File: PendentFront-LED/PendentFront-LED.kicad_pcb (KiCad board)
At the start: 2 copper layers, 25.7 x 39.2 mm, 98 parts, among them J1 Conn_01x05_Pin, U1 74VHC9595FT, U2 74VHC9595FT, U3 74VHC9595FT, U4 74VHC9595FT

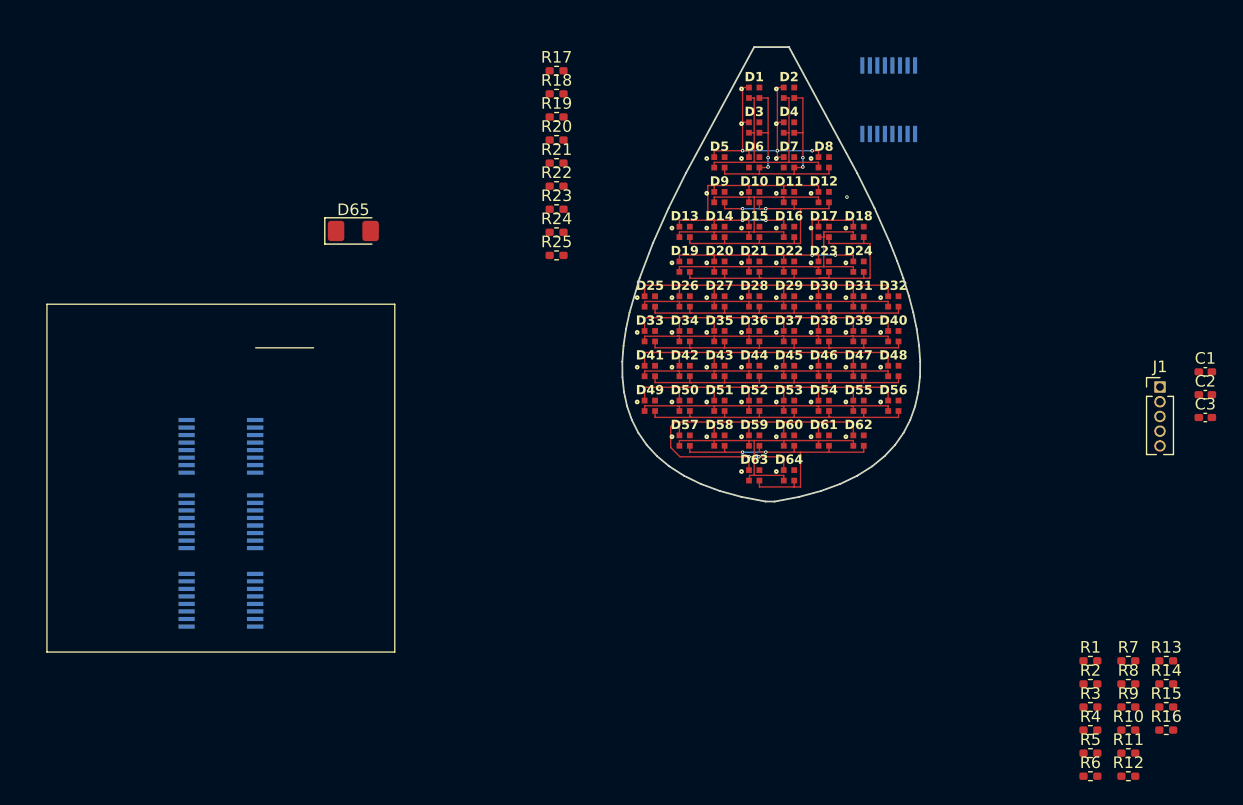
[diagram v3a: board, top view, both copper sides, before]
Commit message: Connected up shift registers. Still need to rearrange connections to make routing possible
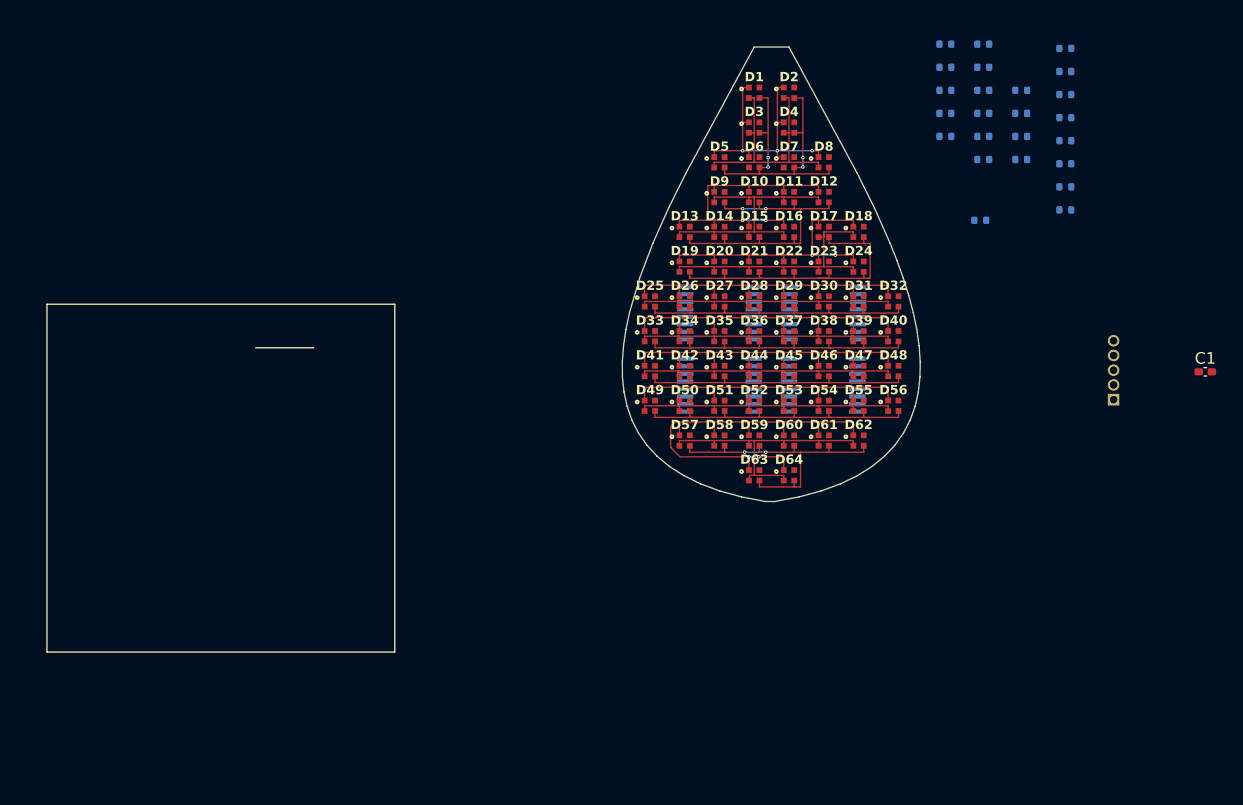
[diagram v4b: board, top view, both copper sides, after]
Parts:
- removed C2, C3: 1uF, Capacitor_SMD:C_0402_1005Metric_Pad0.74x0.62mm_HandSolder
- removed D65: AUX, LED_SMD:LED_1206_3216Metric_Pad1.42x1.75mm_HandSolder
- removed R25: R, Resistor_SMD:R_0402_1005Metric_Pad0.72x0.64mm_HandSolder
- J1: moved to B.Cu
- R1, R10, R11, R12, R13, R14, R15, R16, R17, R18, R19, R2, R20, R21, R22, R23, R24, R3, R4, R5, R6, R7, R8, R9: footprint Resistor_SMD:R_0402_1005Metric_Pad0.72x0.64mm_HandSolder -> Resistor_SMD:R_0402_1005Metric; moved to B.Cu
- moved R12 64.4 mm to (132.8, 47.8)
- moved R6 64.4 mm to (129.5, 47.8)
- moved R11 60.5 mm to (132.8, 49.8)
- moved R5 60.5 mm to (129.5, 49.8)
- moved R10 56.6 mm to (132.8, 51.8)
- moved R16 56.6 mm to (136.0, 51.8)
- moved R4 56.6 mm to (129.5, 51.8)
- moved U3 53.3 mm to (119.0, 77.2), turned to 180 degrees
- moved U4 53.3 mm to (119.0, 71.0), turned to 180 degrees
- moved R9 52.7 mm to (132.8, 53.8)
- moved R15 52.7 mm to (136.0, 53.8)
- moved R3 52.7 mm to (129.5, 53.8)
- moved U2 49.6 mm to (110.0, 71.0), turned to 180 degrees
- moved R14 48.9 mm to (136.0, 55.8)
- moved R2 48.9 mm to (129.5, 55.8)
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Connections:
- U1 pad 10: unconnected-(U1-Q5-Pad10) -> /ROW5
- U1 pad 11: unconnected-(U1-Q6-Pad11) -> /ROW6
- U1 pad 12: unconnected-(U1-Q7-Pad12) -> /ROW7
- U1 pad 13: unconnected-(U1-Q8-Pad13) -> /ROW8
- U1 pad 5: unconnected-(U1-Q1-Pad5) -> /ROW1
- U1 pad 6: unconnected-(U1-Q2-Pad6) -> /ROW2
- U1 pad 7: unconnected-(U1-Q3-Pad7) -> /ROW3
- U1 pad 9: unconnected-(U1-Q4-Pad9) -> /ROW4
- U2 pad 10: unconnected-(U2-Q5-Pad10) -> /COLOR.RED5
- U2 pad 11: unconnected-(U2-Q6-Pad11) -> /COLOR.RED6
- U2 pad 12: unconnected-(U2-Q7-Pad12) -> /COLOR.RED7
- U2 pad 13: unconnected-(U2-Q8-Pad13) -> /COLOR.RED8
- U2 pad 5: unconnected-(U2-Q1-Pad5) -> /COLOR.RED1
- U2 pad 6: unconnected-(U2-Q2-Pad6) -> /COLOR.RED2
- U2 pad 7: unconnected-(U2-Q3-Pad7) -> /COLOR.RED3
- U2 pad 9: unconnected-(U2-Q4-Pad9) -> /COLOR.RED4
- U3 pad 10: unconnected-(U3-Q5-Pad10) -> /COLOR.GREEN5
- U3 pad 11: unconnected-(U3-Q6-Pad11) -> /COLOR.GREEN6
- U3 pad 12: unconnected-(U3-Q7-Pad12) -> /COLOR.GREEN7
- U3 pad 13: unconnected-(U3-Q8-Pad13) -> /COLOR.GREEN8
- U3 pad 5: unconnected-(U3-Q1-Pad5) -> /COLOR.GREEN1
- U3 pad 6: unconnected-(U3-Q2-Pad6) -> /COLOR.GREEN2
- U3 pad 7: unconnected-(U3-Q3-Pad7) -> /COLOR.GREEN3
- U3 pad 9: unconnected-(U3-Q4-Pad9) -> /COLOR.GREEN4
- U4 pad 10: unconnected-(U4-Q5-Pad10) -> /COLOR.BLUE5
- U4 pad 11: unconnected-(U4-Q6-Pad11) -> /COLOR.BLUE6
- U4 pad 12: unconnected-(U4-Q7-Pad12) -> /COLOR.BLUE7
- U4 pad 13: unconnected-(U4-Q8-Pad13) -> /COLOR.BLUE8
- U4 pad 5: unconnected-(U4-Q1-Pad5) -> /COLOR.BLUE1
- U4 pad 6: unconnected-(U4-Q2-Pad6) -> /COLOR.BLUE2
- U4 pad 7: unconnected-(U4-Q3-Pad7) -> /COLOR.BLUE3
- U4 pad 9: unconnected-(U4-Q4-Pad9) -> /COLOR.BLUE4
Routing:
- net (no net): vias 1 -> 0

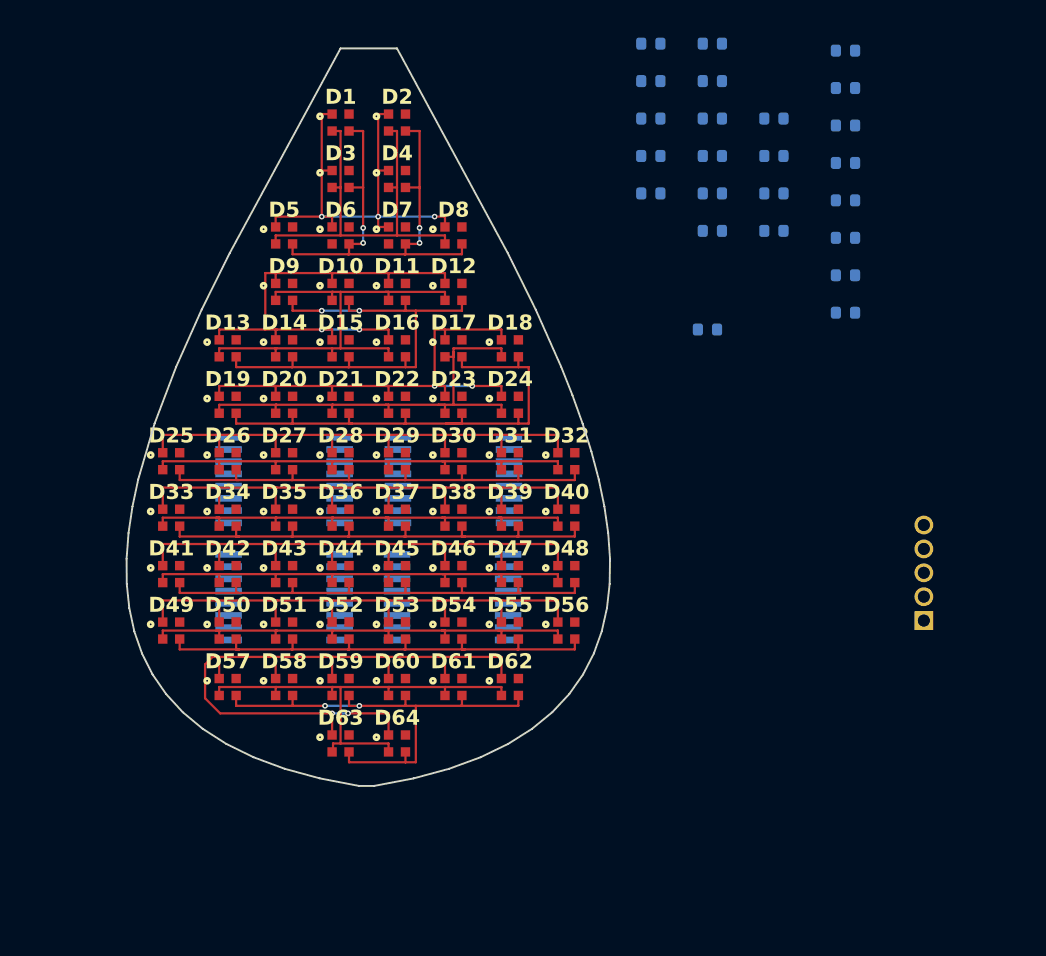
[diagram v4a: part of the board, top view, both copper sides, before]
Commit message: More work on routing the front LED panel
Got through 2 1/2 groups of LEDs and reconfigured connections to shift registers to make routing easier. Split header into 2 groups for easier placement
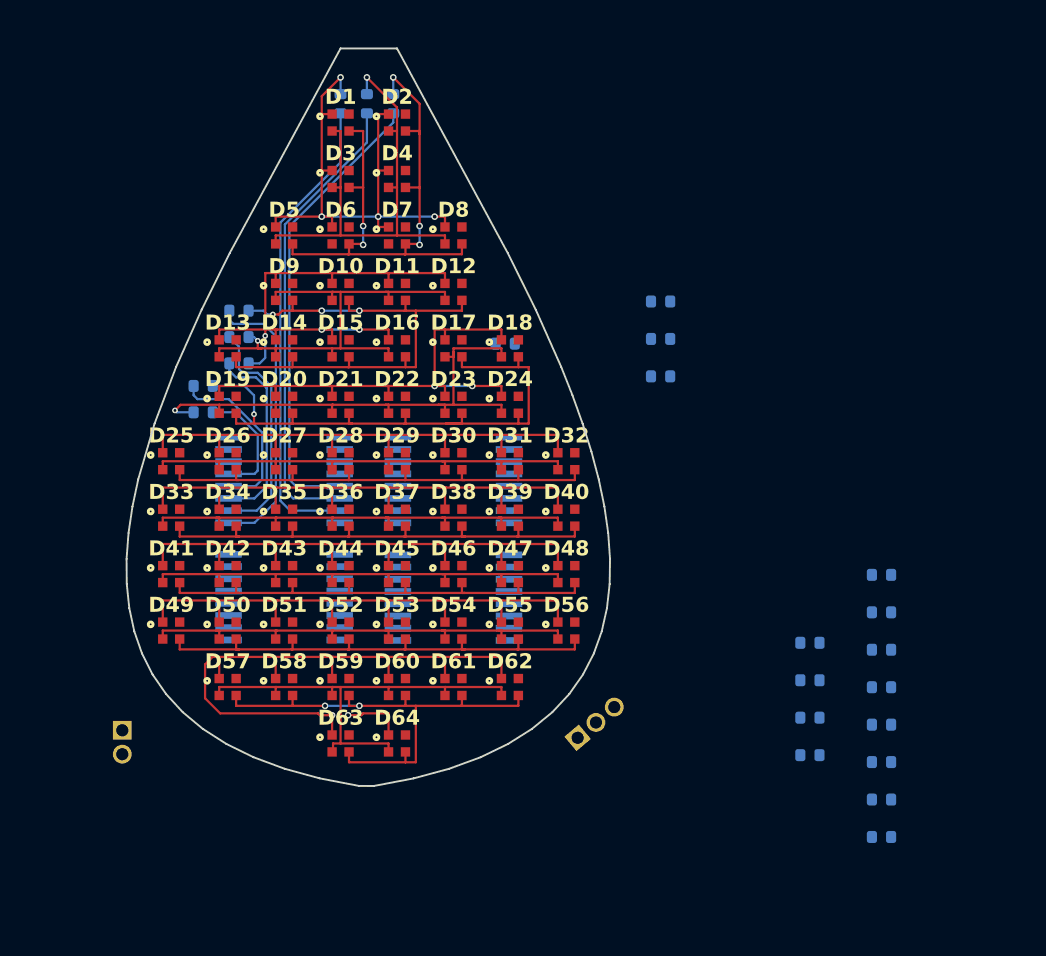
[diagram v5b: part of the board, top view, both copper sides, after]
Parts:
- added J2: Conn_01x02_Pin, Connector_PinHeader_1.27mm:PinHeader_1x02_P1.27mm_Vertical, B.Cu at (101.4, 84.3)
- J1: value Conn_01x05_Pin -> Conn_01x03_Pin; footprint Connector_PinHeader_1.27mm:PinHeader_1x05_P1.27mm_Vertical -> Connector_PinHeader_1.27mm:PinHeader_1x03_P1.27mm_Vertical
- moved R9 29.7 mm to (105.7, 66.0), turned to 180 degrees
- moved R8 29.5 mm to (105.7, 67.4)
- moved R13 27.9 mm to (137.9, 85.6)
- moved R16 27.9 mm to (137.9, 79.7)
- moved R18 27.9 mm to (141.8, 88.0)
- moved R21 27.9 mm to (141.8, 82.0)
- moved R24 27.9 mm to (141.8, 76.0)
- moved R15 27.9 mm to (137.9, 81.6)
- moved R17 27.9 mm to (141.8, 90.0)
- moved R20 27.9 mm to (141.8, 84.0)
- moved R22 27.9 mm to (141.8, 80.0)
- moved R23 27.9 mm to (141.8, 78.0)
- moved R14 27.9 mm to (137.9, 83.6)
- moved R19 27.9 mm to (141.8, 86.0)
- moved R6 26.1 mm to (107.6, 62.0), turned to 180 degrees
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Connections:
- J1 pad 1: VCC -> SerialIn
- J1 pad 2: CLK -> RCK
- J1 pad 3: RCK -> CLK
- U1 pad 3: CLK -> RCK
- U2 pad 10: /COLOR.RED5 -> /COLOR.GREEN2
- U2 pad 11: /COLOR.RED6 -> /COLOR.BLUE2
- U2 pad 12: /COLOR.RED7 -> /COLOR.RED3
- U2 pad 13: /COLOR.RED8 -> /COLOR.GREEN3
- U2 pad 3: CLK -> RCK
- U2 pad 6: /COLOR.RED2 -> /COLOR.GREEN1
- U2 pad 7: /COLOR.RED3 -> /COLOR.BLUE1
- U2 pad 9: /COLOR.RED4 -> /COLOR.RED2
- U3 pad 10: /COLOR.GREEN5 -> /COLOR.RED5
- U3 pad 11: /COLOR.GREEN6 -> /COLOR.GREEN5
- U3 pad 12: /COLOR.GREEN7 -> /COLOR.BLUE5
- U3 pad 13: /COLOR.GREEN8 -> /COLOR.RED6
- U3 pad 3: CLK -> RCK
- U3 pad 5: /COLOR.GREEN1 -> /COLOR.BLUE3
- U3 pad 6: /COLOR.GREEN2 -> /COLOR.RED4
- U3 pad 7: /COLOR.GREEN3 -> /COLOR.GREEN4
- U3 pad 9: /COLOR.GREEN4 -> /COLOR.BLUE4
- U4 pad 10: /COLOR.BLUE5 -> /COLOR.BLUE7
- U4 pad 11: /COLOR.BLUE6 -> /COLOR.RED8
- U4 pad 12: /COLOR.BLUE7 -> /COLOR.GREEN8
- U4 pad 3: CLK -> RCK
- U4 pad 5: /COLOR.BLUE1 -> /COLOR.GREEN6
- U4 pad 6: /COLOR.BLUE2 -> /COLOR.BLUE6
- U4 pad 7: /COLOR.BLUE3 -> /COLOR.RED7
- U4 pad 9: /COLOR.BLUE4 -> /COLOR.GREEN7
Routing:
- net /COLOR.BLUE1: track 0.00 -> 25.3 mm
- net /COLOR.GREEN1: track 0.00 -> 24.9 mm
- net /COLOR.RED1: track 0.00 -> 24.6 mm
- net /COLOR.RED2: track 0.00 -> 15.1 mm
- net /COLOR.GREEN2: track 0.00 -> 12.4 mm
- net /COLOR.BLUE2: track 0.00 -> 10.3 mm
- net /COLOR.RED3: track 0.00 -> 9.38 mm
- net /COLOR.GREEN3: track 0.00 -> 6.42 mm
- net Net-(D1-Pad3): track 27.8 -> 32.4 mm, vias 4 -> 5
- net Net-(D1-Pad2): track 22.8 -> 27.2 mm, vias 0 -> 1
- net Net-(D17-Pad3): track 27.6 -> 31.5 mm, vias 0 -> 1
- net Net-(D17-Pad2): track 25.0 -> 28.5 mm, vias 0 -> 1
- net Net-(D1-Pad1): track 25.5 -> 28.7 mm, vias 3 -> 4
- net Net-(D10-Pad1): track 26.7 -> 29.2 mm, vias 2 -> 3
- net Net-(D10-Pad3): track 26.7 -> 29.2 mm, vias 2 -> 3
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
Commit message: routing
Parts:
- moved R12 9.50 mm to (121.5, 65.8)
- moved R10 8.94 mm to (121.5, 62.8), turned to 180 degrees
- moved R11 8.53 mm to (121.5, 64.2)
- moved R7 3.51 mm to (121.5, 67.2)
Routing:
- net /COLOR.BLUE4: track 0.00 -> 14.3 mm
- net /COLOR.GREEN4: track 0.00 -> 12.4 mm
- net /COLOR.RED4: track 0.00 -> 10.6 mm
- net Net-(D25-Pad3): track 25.9 -> 34.2 mm, vias 0 -> 1
- net /COLOR.BLUE3: track 0.00 -> 7.85 mm
- net Net-(D25-Pad2): track 25.3 -> 32.3 mm, vias 0 -> 1
- net Net-(D25-Pad1): track 29.5 -> 36.3 mm, vias 0 -> 1
- net Net-(D17-Pad1): track 27.0 -> 28.3 mm, vias 2 -> 1
- net Net-(D17-Pad2): track 28.5 -> 28.8 mm, vias 1 -> 3

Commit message: More routing
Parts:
- moved R24 26.3 mm to (119.8, 90.6)
- moved R23 24.4 mm to (119.9, 89.0)
- moved R19 24.3 mm to (118.0, 80.8), turned to 180 degrees
- moved R20 23.8 mm to (118.0, 82.2), turned to 180 degrees
- moved R22 22.4 mm to (120.4, 86.8)
- moved C1 21.2 mm to (130.8, 74.8)
- moved R17 20.8 mm to (125.0, 77.6), turned to 180 degrees
- moved R21 20.6 mm to (121.2, 80.8), turned to 180 degrees
- moved R18 20.5 mm to (125.0, 76.2), turned to 180 degrees
- moved R13 18.8 mm to (125.0, 72.0), turned to 180 degrees
- moved J1 16.5 mm to (109.1, 84.5), turned to 62.5 degrees
- moved R14 16.5 mm to (125.0, 73.4), turned to 180 degrees
- moved R15 14.6 mm to (125.0, 74.8), turned to 180 degrees
- moved R16 13.0 mm to (125.0, 79.0), turned to 180 degrees
- moved J2 4.35 mm to (104.6, 81.4), turned to 35 degrees
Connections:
- U3 pad 13: /COLOR.RED6 -> /COLOR.BLUE4
- U3 pad 9: /COLOR.BLUE4 -> /COLOR.RED6
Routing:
- net VCC: track 0.00 -> 18.0 mm
- net /COLOR.BLUE5: track 0.00 -> 10.6 mm
- net /COLOR.GREEN5: track 0.00 -> 9.66 mm
- net /COLOR.RED6: track 0.00 -> 9.65 mm
- net /COLOR.RED5: track 0.00 -> 9.34 mm
- net Net-(D41-Pad1): track 30.6 -> 37.9 mm, vias 0 -> 1
- net Net-(D57-Pad1): track 36.6 -> 29.8 mm, vias 2 -> 3
- net Net-(D41-Pad2): track 25.3 -> 29.6 mm, vias 0 -> 1
- net /COLOR.GREEN7: track 0.00 -> 3.96 mm
- net Net-(D49-Pad2): track 25.3 -> 28.7 mm, vias 0 -> 1
- net Net-(D49-Pad1): track 30.6 -> 33.8 mm, vias 0 -> 1
- net /COLOR.BLUE7: track 0.00 -> 3.12 mm
- net /COLOR.RED7: track 0.00 -> 2.93 mm
- net /COLOR.BLUE6: track 0.00 -> 2.86 mm
- net Net-(D33-Pad2): track 25.3 -> 27.9 mm, vias 0 -> 1
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
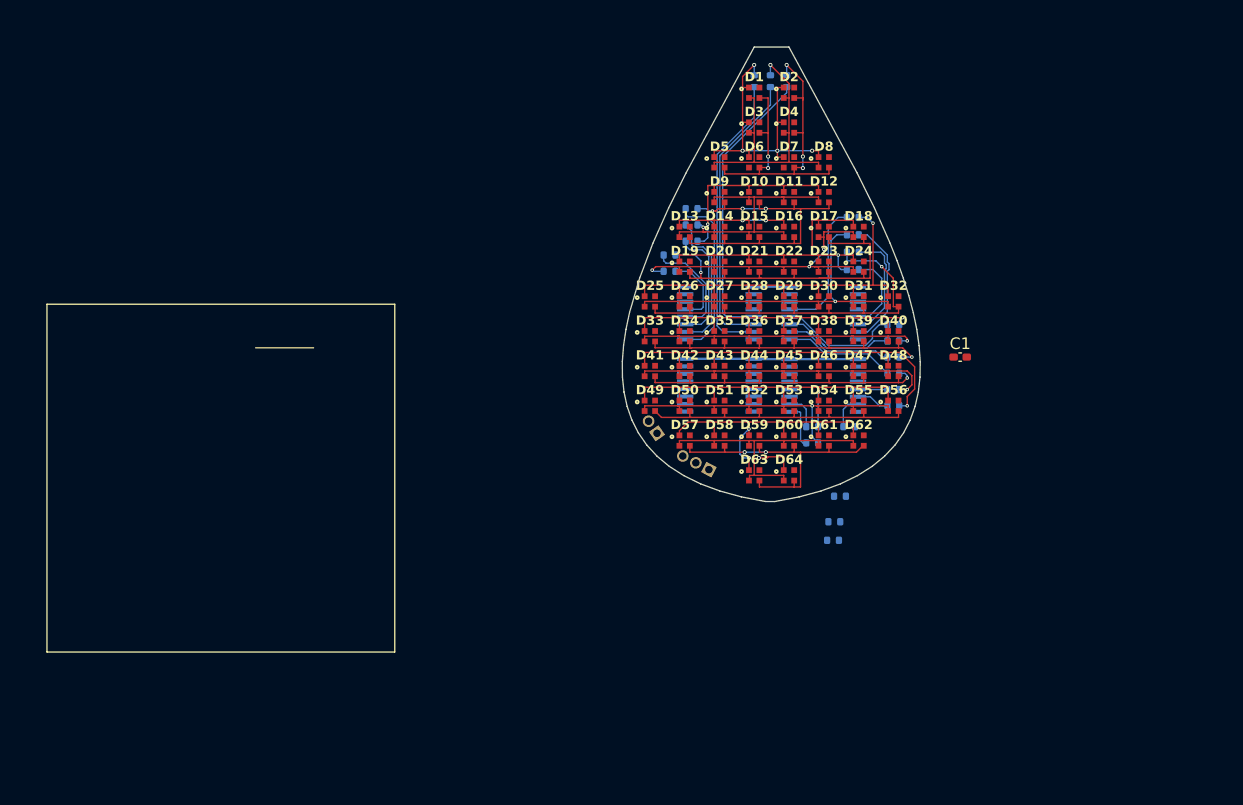
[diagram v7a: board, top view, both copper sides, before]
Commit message: More routing, started putting row lines around the outside of the pendent
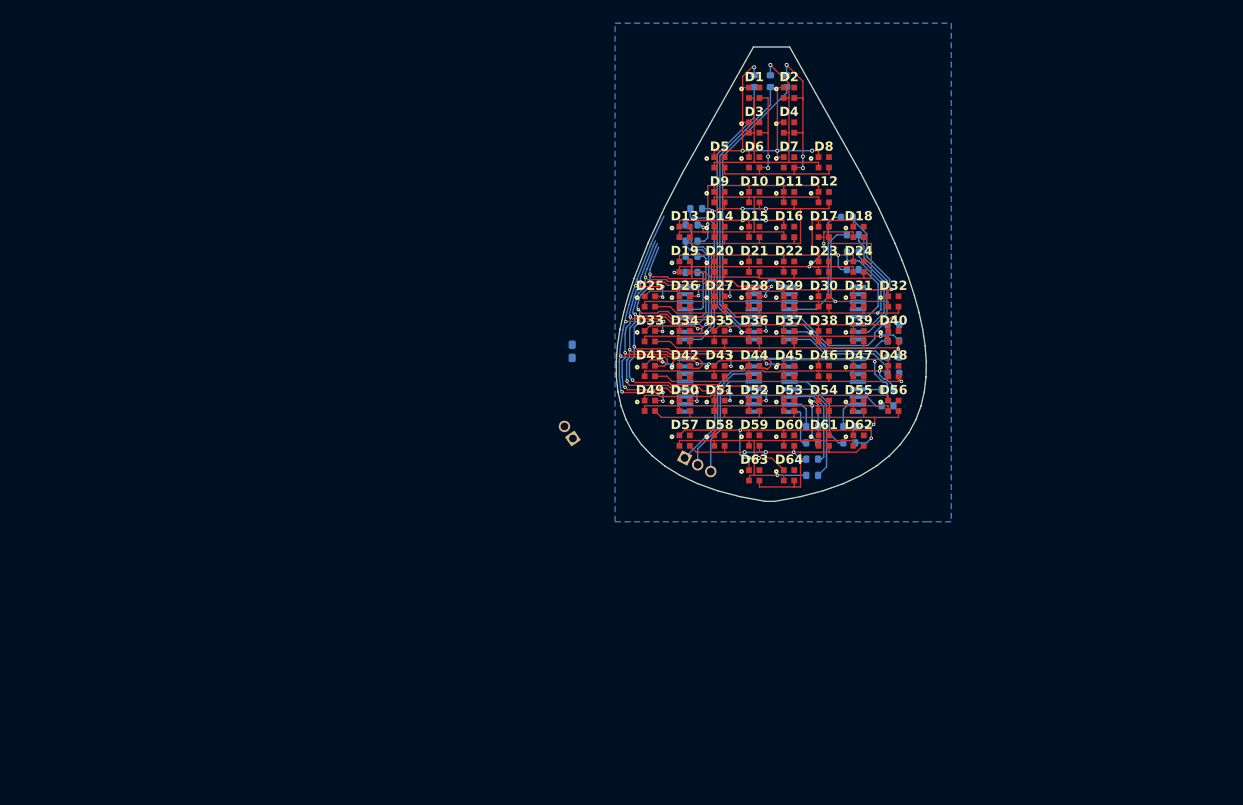
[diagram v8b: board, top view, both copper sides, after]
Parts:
- C1: moved to B.Cu
- moved C1 33.5 mm to (97.3, 74.3), turned to 90 degrees
- moved J2 7.27 mm to (97.4, 81.8)
- moved R24 7.23 mm to (118.0, 83.6)
- moved R22 4.67 mm to (121.2, 82.2), turned to 180 degrees
- moved R23 4.43 mm to (118.0, 85.0)
- moved J1 2.32 mm to (107.0, 83.5), turned to -117.5 degrees
- moved R8 1.90 mm to (107.6, 67.5)
- moved R9 1.90 mm to (107.6, 66.1), turned to 0 degrees
- moved R10 0.50 mm to (121.0, 62.8)
- moved R16 0.50 mm to (124.5, 79.0)
- moved R17 0.50 mm to (124.5, 77.6)
- moved R6 0.40 mm to (108.0, 62.0)
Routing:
- net /ROW4: track 0.00 -> 65.4 mm, vias 0 -> 10
- net /ROW3: track 0.00 -> 52.2 mm, vias 0 -> 12
- net /ROW2: track 0.00 -> 45.1 mm, vias 0 -> 8
- net /ROW1: track 0.00 -> 35.4 mm, vias 0 -> 10
- net SerialIn: track 0.00 -> 11.2 mm
- net RCK: track 0.00 -> 10.9 mm
- net CLK: track 0.00 -> 10.5 mm
- net /COLOR.GREEN8: track 0.00 -> 10.1 mm
- net /COLOR.BLUE8: track 0.00 -> 8.32 mm
- net /COLOR.RED8: track 0.00 -> 8.24 mm
- net Net-(D41-Pad1): track 37.9 -> 30.8 mm, vias 1 -> 7
- net Net-(D49-Pad1): track 33.8 -> 28.0 mm
- net VCC: track 18.0 -> 12.6 mm
- net Net-(D33-Pad1): track 32.6 -> 27.3 mm, vias 1 -> 3
- net Net-(D25-Pad1): track 36.3 -> 33.6 mm
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- added copper zone on B.Cu, net GND
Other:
- board size 25.7 x 39.2 mm -> 26.7 x 39.2 mm
